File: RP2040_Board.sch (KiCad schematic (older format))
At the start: 0 parts

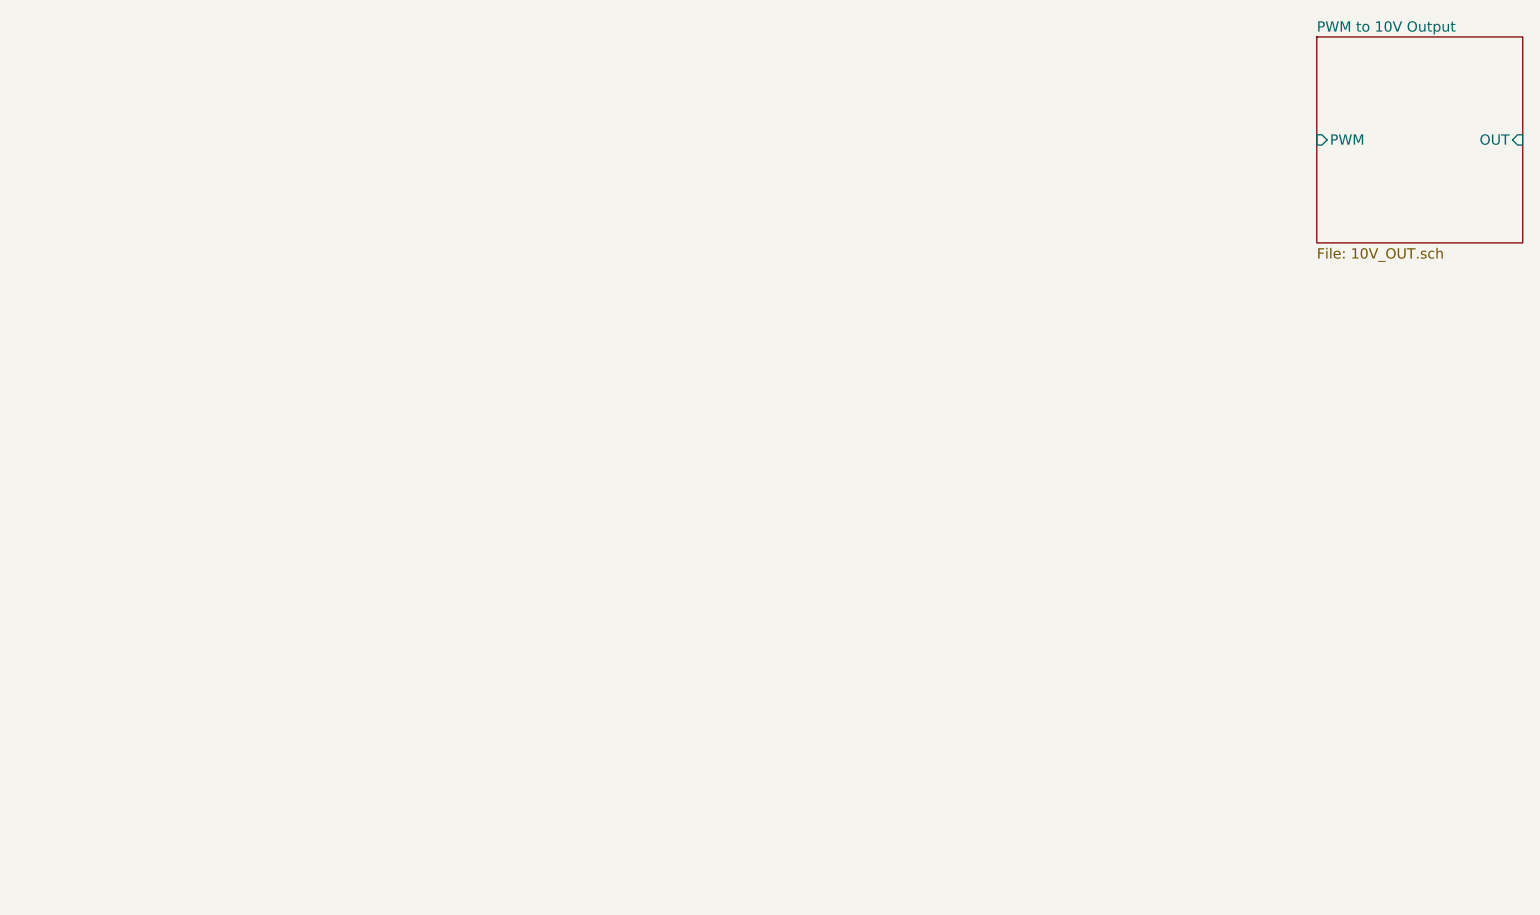
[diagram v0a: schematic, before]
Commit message: Added a library for the Pi Pico
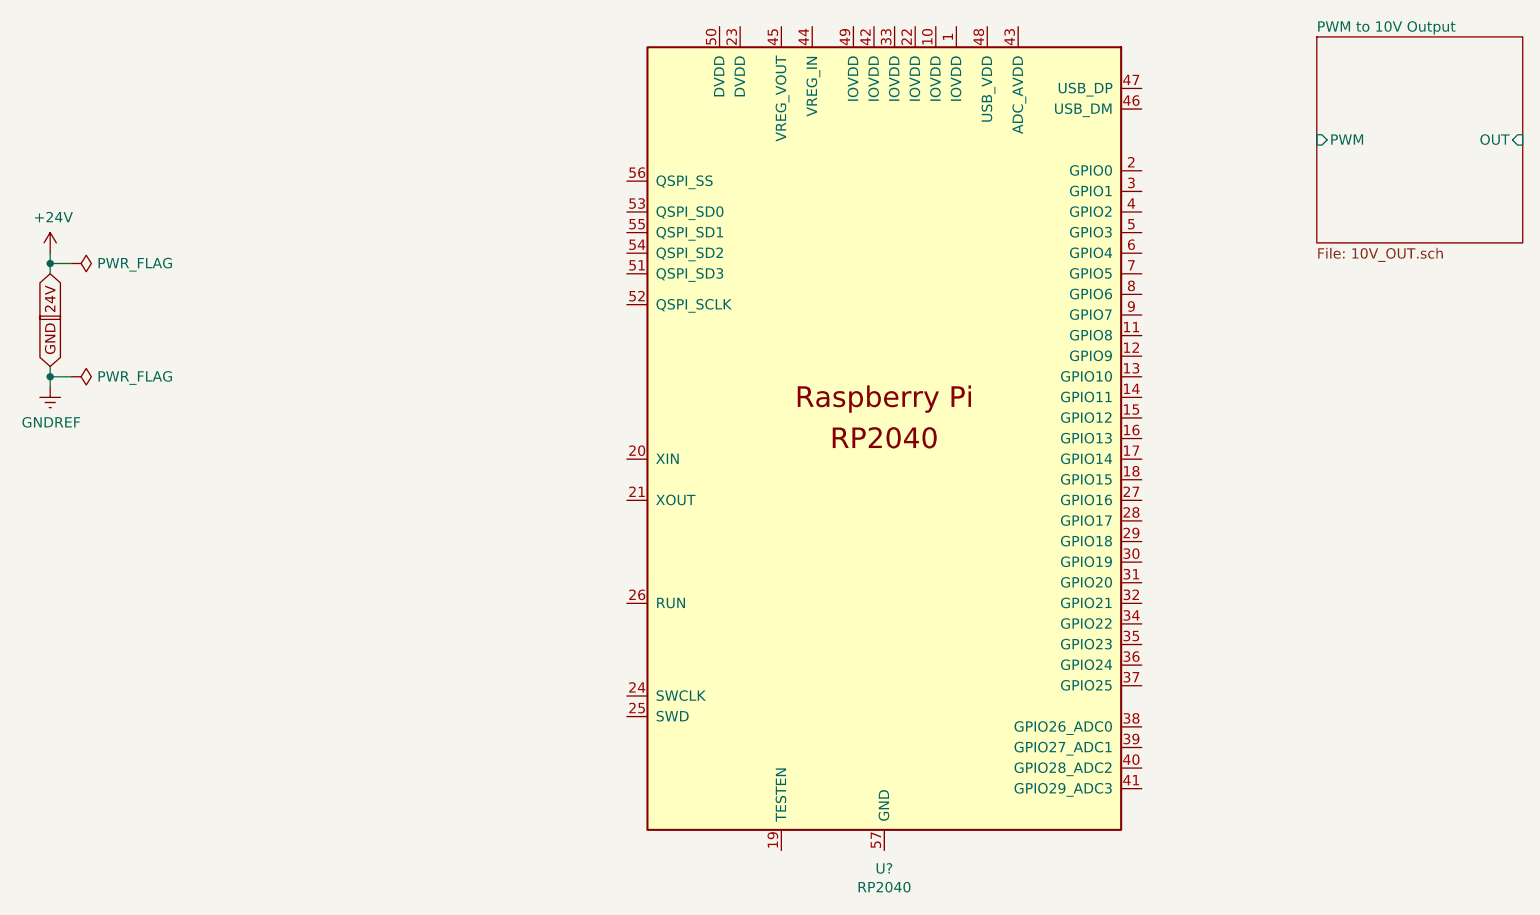
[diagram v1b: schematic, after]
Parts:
- added U?: RP2040, RP2040_minimal:RP2040-QFN-56, symbol MCU_RaspberryPi_and_Boards:RP2040
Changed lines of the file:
@@
 F3 "OUT" I R 8600 2450 50
 $EndSheet
+$Comp
+L power:GNDREF #PWR0101
+U 1 1 60A8290A
+P 1450 3650
+F 0 "#PWR0101" H 1450 3400 50  0001 C CNN
+F 1 "GNDREF" H 1455 3477 50  0000 C CNN
+F 2 "" H 1450 3650 50  0001 C CNN
+F 3 "" H 1450 3650 50  0001 C CNN
+	1    1450 3650
+	1    0    0    -1
+$EndComp
+$Comp
+L power:+24V #PWR0102
+U 1 1 60A8325F
+P 1450 3000
+F 0 "#PWR0102" H 1450 2850 50  0001 C CNN
+F 1 "+24V" H 1465 3173 50  0000 C CNN
+F 2 "" H 1450 3000 50  0001 C CNN
+F 3 "" H 1450 3000 50  0001 C CNN
+	1    1450 3000
+	1    0    0    -1
+$EndComp
+Text GLabel 1450 3100 3    50   Input ~ 0
+24V
+Text GLabel 1450 3550 1    50   Input ~ 0
+GND
+Wire Wire Line
+	1450 3000 1450 3050
+Wire Wire Line
+	1450 3650 1450 3600
+$Comp
+L power:PWR_FLAG #FLG0101
+U 1 1 60A8412B
+P 1550 3050
+F 0 "#FLG0101" H 1550 3125 50  0001 C CNN
+F 1 "PWR_FLAG" V 1550 3178 50  0000 L CNN
+F 2 "" H 1550 3050 50  0001 C CNN
+F 3 "~" H 1550 3050 50  0001 C CNN
+	1    1550 3050
+	0    1    1    0
+$EndComp
+$Comp
+L power:PWR_FLAG #FLG0102
+U 1 1 60A849AB
+P 1550 3600
+F 0 "#FLG0102" H 1550 3675 50  0001 C CNN
+F 1 "PWR_FLAG" V 1550 3728 50  0000 L CNN
+F 2 "" H 1550 3600 50  0001 C CNN
+F 3 "~" H 1550 3600 50  0001 C CNN
+	1    1550 3600
+	0    1    1    0
+$EndComp
+Wire Wire Line
+	1550 3050 1450 3050
+Connection ~ 1450 3050
+Wire Wire Line
+	1450 3050 1450 3100
+Wire Wire Line
+	1550 3600 1450 3600
+Connection ~ 1450 3600
+Wire Wire Line
+	1450 3600 1450 3550
+$Comp
+L MCU_RaspberryPi_and_Boards:RP2040 U?
+U 1 1 60A88326
+P 5500 3900
+F 0 "U?" H 5500 1811 50  0000 C CNN
+F 1 "RP2040" H 5500 1720 50  0000 C CNN
+F 2 "RP2040_minimal:RP2040-QFN-56" H 4750 3900 50  0001 C CNN
+F 3 "" H 4750 3900 50  0001 C CNN
+	1    5500 3900
+	1    0    0    -1
+$EndComp
 $EndSCHEMATC

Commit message: 10V Input Circuit First Revision
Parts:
- removed U?: RP2040, RP2040_minimal:RP2040-QFN-56, symbol MCU_RaspberryPi_and_Boards:RP2040
- added U2: Pico, MCU_RaspberryPi_and_Boards:RPi_Pico_SMD_TH, symbol MCU_RaspberryPi_and_Boards:Pico
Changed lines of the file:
@@
 $Descr A4 11693 8268
 encoding utf-8
-Sheet 1 2
+Sheet 1 3
 Title "Pi Pico Test Board"
 Date "2021-05-20"
@@
 $EndDescr
 $Sheet
-S 7600 1950 1000 1000
+S 7700 2450 600  600
 U 60A68B69
 F0 "PWM to 10V Output" 50
 F1 "10V_OUT.sch" 50
-F2 "PWM" I L 7600 2450 50
-F3 "OUT" I R 8600 2450 50
+F2 "PWM" I L 7700 2750 50
+F3 "OUT" I R 8300 2750 50
 $EndSheet
 $Comp
@@
 	1450 3600 1450 3550
 $Comp
-L MCU_RaspberryPi_and_Boards:RP2040 U?
-U 1 1 60A88326
-P 5500 3900
-F 0 "U?" H 5500 1811 50  0000 C CNN
-F 1 "RP2040" H 5500 1720 50  0000 C CNN
-F 2 "RP2040_minimal:RP2040-QFN-56" H 4750 3900 50  0001 C CNN
-F 3 "" H 4750 3900 50  0001 C CNN
-	1    5500 3900
+L MCU_RaspberryPi_and_Boards:Pico U2
+U 1 1 60A8B6FD
+P 5750 3500
+F 0 "U2" H 5750 4715 50  0000 C CNN
+F 1 "Pico" H 5750 4624 50  0000 C CNN
+F 2 "MCU_RaspberryPi_and_Boards:RPi_Pico_SMD_TH" V 5750 3500 50  0001 C CNN
+F 3 "" H 5750 3500 50  0001 C CNN
+	1    5750 3500
 	1    0    0    -1
 $EndComp
+$Sheet
+S 7700 3300 600  600
+U 60A8EFC5
+F0 "10V to 3.3V Input" 50
+F1 "10V_IN.sch" 50
+F2 "OUT" I R 8300 3600 50
+F3 "IN" I L 7700 3600 50
+$EndSheet
+$Comp
+L power:+5V #PWR?
+U 1 1 60A9FB68
+P 2200 3000
+F 0 "#PWR?" H 2200 2850 50  0001 C CNN
+F 1 "+5V" H 2215 3173 50  0000 C CNN
+F 2 "" H 2200 3000 50  0001 C CNN
+F 3 "" H 2200 3000 50  0001 C CNN
+	1    2200 3000
+	1    0    0    -1
+$EndComp
+Text GLabel 2200 3100 3    50   Input ~ 0
+5V
+Wire Wire Line
+	2200 3000 2200 3050
+$Comp
+L power:PWR_FLAG #FLG?
+U 1 1 60AA0BC3
+P 2300 3050
+F 0 "#FLG?" H 2300 3125 50  0001 C CNN
+F 1 "PWR_FLAG" V 2300 3178 50  0000 L CNN
+F 2 "" H 2300 3050 50  0001 C CNN
+F 3 "~" H 2300 3050 50  0001 C CNN
+	1    2300 3050
+	0    1    1    0
+$EndComp
+Wire Wire Line
+	2300 3050 2200 3050
+Connection ~ 2200 3050
+Wire Wire Line
+	2200 3050 2200 3100
 $EndSCHEMATC

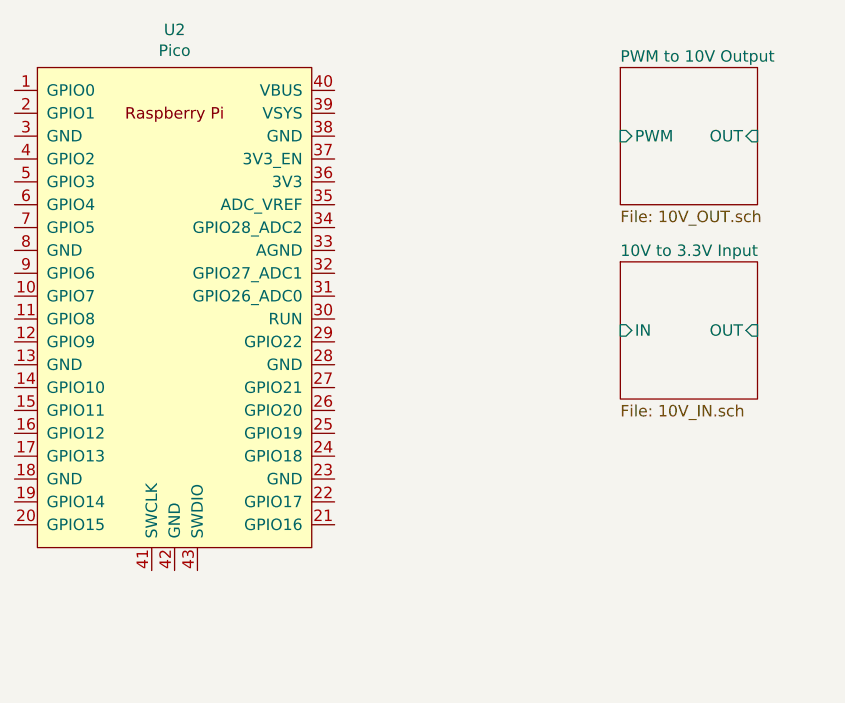
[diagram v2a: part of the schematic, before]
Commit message: Added PWM to 20mA Output Subcircuit
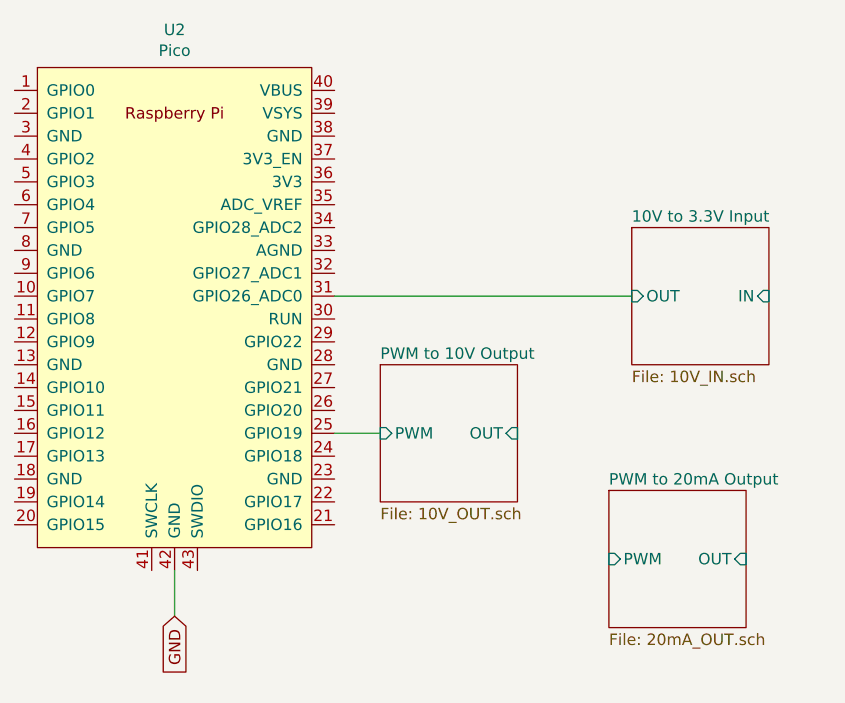
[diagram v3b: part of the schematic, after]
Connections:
- net 10V to 3.3V Input/OUT: now also U2.31 (GPIO26_ADC0)
- net GNDREF: now also U2.42 (GND)
- net PWM to 10V Output/PWM: now also U2.25 (GPIO19)
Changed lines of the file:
@@
 $Descr A4 11693 8268
 encoding utf-8
-Sheet 1 3
+Sheet 1 4
 Title "Pi Pico Test Board"
 Date "2021-05-20"
@@
 $EndDescr
 $Sheet
-S 7700 2450 600  600
+S 6650 3750 600  600
 U 60A68B69
 F0 "PWM to 10V Output" 50
 F1 "10V_OUT.sch" 50
-F2 "PWM" I L 7700 2750 50
-F3 "OUT" I R 8300 2750 50
+F2 "PWM" I L 6650 4050 50
+F3 "OUT" I R 7250 4050 50
 $EndSheet
 $Comp
@@
 $EndComp
 $Sheet
-S 7700 3300 600  600
+S 7750 3150 600  600
 U 60A8EFC5
 F0 "10V to 3.3V Input" 50
 F1 "10V_IN.sch" 50
-F2 "OUT" I R 8300 3600 50
-F3 "IN" I L 7700 3600 50
+F2 "OUT" I L 7750 3450 50
+F3 "IN" I R 8350 3450 50
 $EndSheet
 $Comp
-L power:+5V #PWR?
+L power:+5V #PWR0103
 U 1 1 60A9FB68
 P 2200 3000
-F 0 "#PWR?" H 2200 2850 50  0001 C CNN
+F 0 "#PWR0103" H 2200 2850 50  0001 C CNN
 F 1 "+5V" H 2215 3173 50  0000 C CNN
 F 2 "" H 2200 3000 50  0001 C CNN
@@
 	2200 3000 2200 3050
 $Comp
-L power:PWR_FLAG #FLG?
+L power:PWR_FLAG #FLG0103
 U 1 1 60AA0BC3
 P 2300 3050
-F 0 "#FLG?" H 2300 3125 50  0001 C CNN
+F 0 "#FLG0103" H 2300 3125 50  0001 C CNN
 F 1 "PWR_FLAG" V 2300 3178 50  0000 L CNN
 F 2 "" H 2300 3050 50  0001 C CNN
@@
 Wire Wire Line
 	2200 3050 2200 3100
+Wire Wire Line
+	6450 4050 6650 4050
+Wire Wire Line
+	6450 3450 7750 3450
+Text GLabel 5750 4850 3    50   Input ~ 0
+GND
+Wire Wire Line
+	5750 4850 5750 4650
+$Sheet
+S 7650 4300 600  600
+U 60ABD2CD
+F0 "PWM to 20mA Output" 50
+F1 "20mA_OUT.sch" 50
+F2 "PWM" I L 7650 4600 50
+F3 "OUT" I R 8250 4600 50
+$EndSheet
 $EndSCHEMATC
